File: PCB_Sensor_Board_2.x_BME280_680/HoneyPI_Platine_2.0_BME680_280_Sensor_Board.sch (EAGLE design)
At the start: 4 parts

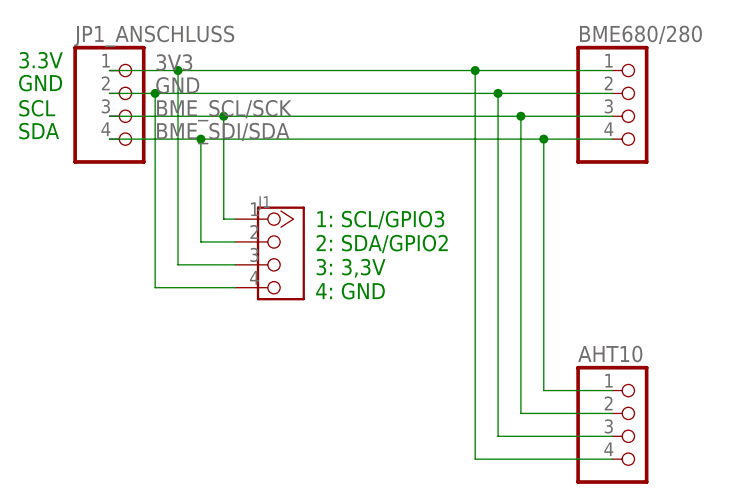
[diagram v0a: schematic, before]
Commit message: 3rd i²C interface
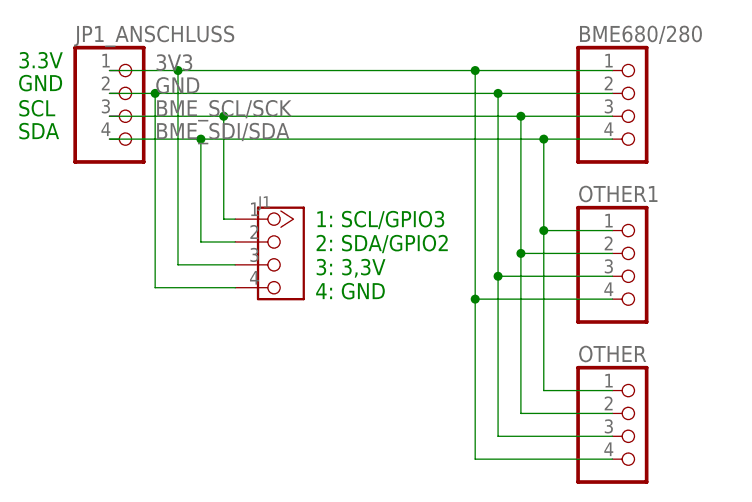
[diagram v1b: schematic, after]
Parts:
- added OTHER1: (no value), pinhead:PINHD-1X4
- renumbered AHT10 to OTHER
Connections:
- net 3V3: now also OTHER1.4
- net BME_SCL/SCK: now also OTHER1.2
- net BME_SDI/SDA: now also OTHER1.1
- net GND: now also OTHER1.3
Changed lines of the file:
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@@
 <part name="BME680/280" library="pinhead" library_urn="urn:adsk.eagle:library:325" deviceset="PINHD-1X4" device="" package3d_urn="urn:adsk.eagle:package:22407/2"/>
 <part name="JP1_ANSCHLUSS" library="pinhead" library_urn="urn:adsk.eagle:library:325" deviceset="PINHD-1X4" device="" package3d_urn="urn:adsk.eagle:package:22407/2"/>
-<part name="AHT10" library="pinhead" library_urn="urn:adsk.eagle:library:325" deviceset="PINHD-1X4" device="" package3d_urn="urn:adsk.eagle:package:22407/2"/>
+<part name="OTHER" library="pinhead" library_urn="urn:adsk.eagle:library:325" deviceset="PINHD-1X4" device="" package3d_urn="urn:adsk.eagle:package:22407/2"/>
 <part name="J1" library="Connector" deviceset="TWIG-4P-2.0" device="-2.0"/>
 <part name="FRAME1" library="frames" library_urn="urn:adsk.eagle:library:229" deviceset="DINA4_L" device=""/>
+<part name="OTHER1" library="pinhead" library_urn="urn:adsk.eagle:library:325" deviceset="PINHD-1X4" device="" package3d_urn="urn:adsk.eagle:package:22407/2"/>
 </parts>
 <sheets>
@@
 <attribute name="VALUE" x="-247.65" y="104.14" size="1.778" layer="96"/>
 </instance>
-<instance part="AHT10" gate="A" x="-185.42" y="76.2" smashed="yes" grouprefs="I²C-G1">
+<instance part="OTHER" gate="A" x="-185.42" y="76.2" smashed="yes" grouprefs="I²C-G1">
 <attribute name="NAME" x="-191.77" y="84.455" size="1.778" layer="95"/>
 <attribute name="VALUE" x="-191.77" y="68.58" size="1.778" layer="96"/>
@@
 <attribute name="DRAWING_NAME" x="-170.18" y="29.21" size="2.54" layer="94"/>
 </instance>
+<instance part="OTHER1" gate="A" x="-185.42" y="93.98" smashed="yes">
+<attribute name="NAME" x="-191.77" y="102.235" size="1.778" layer="95"/>
+<attribute name="VALUE" x="-191.77" y="86.36" size="1.778" layer="96"/>
+</instance>
 </instances>
 <busses>
@@
 <wire x1="-243.84" y1="111.76" x2="-231.14" y2="111.76" width="0.1524" layer="91" grouprefs="I²C-G1"/>
 <pinref part="BME680/280" gate="A" pin="3"/>
-<pinref part="AHT10" gate="A" pin="2"/>
+<pinref part="OTHER" gate="A" pin="2"/>
 <wire x1="-231.14" y1="111.76" x2="-198.12" y2="111.76" width="0.1524" layer="91" grouprefs="I²C-G1"/>
 <wire x1="-198.12" y1="111.76" x2="-187.96" y2="111.76" width="0.1524" layer="91" grouprefs="I²C-G1"/>
 <wire x1="-198.12" y1="78.74" x2="-187.96" y2="78.74" width="0.1524" layer="91" grouprefs="I²C-G1"/>
-<wire x1="-198.12" y1="78.74" x2="-198.12" y2="111.76" width="0.1524" layer="91" grouprefs="I²C-G1"/>
+<wire x1="-198.12" y1="78.74" x2="-198.12" y2="96.52" width="0.1524" layer="91" grouprefs="I²C-G1"/>
 <junction x="-198.12" y="111.76" grouprefs="I²C-G1"/>
 <pinref part="J1" gate="G$1" pin="1"/>
+<wire x1="-198.12" y1="96.52" x2="-198.12" y2="111.76" width="0.1524" layer="91" grouprefs="I²C-G1"/>
 <wire x1="-231.14" y1="111.76" x2="-231.14" y2="100.33" width="0.1524" layer="91" grouprefs="I²C-G1"/>
 <wire x1="-231.14" y1="100.33" x2="-229.87" y2="100.33" width="0.1524" layer="91" grouprefs="I²C-G1"/>
 <junction x="-231.14" y="111.76" grouprefs="I²C-G1"/>
+<pinref part="OTHER1" gate="A" pin="2"/>
+<wire x1="-187.96" y1="96.52" x2="-198.12" y2="96.52" width="0.1524" layer="91"/>
+<junction x="-198.12" y="96.52"/>
 </segment>
 </net>
@@
 <wire x1="-195.58" y1="109.22" x2="-233.68" y2="109.22" width="0.1524" layer="91" grouprefs="I²C-G1"/>
 <wire x1="-233.68" y1="109.22" x2="-243.84" y2="109.22" width="0.1524" layer="91" grouprefs="I²C-G1"/>
-<wire x1="-195.58" y1="109.22" x2="-195.58" y2="81.28" width="0.1524" layer="91" grouprefs="I²C-G1"/>
+<wire x1="-195.58" y1="109.22" x2="-195.58" y2="99.06" width="0.1524" layer="91" grouprefs="I²C-G1"/>
 <junction x="-195.58" y="109.22" grouprefs="I²C-G1"/>
-<pinref part="AHT10" gate="A" pin="1"/>
+<pinref part="OTHER" gate="A" pin="1"/>
+<wire x1="-195.58" y1="99.06" x2="-195.58" y2="81.28" width="0.1524" layer="91" grouprefs="I²C-G1"/>
 <wire x1="-195.58" y1="81.28" x2="-187.96" y2="81.28" width="0.1524" layer="91" grouprefs="I²C-G1"/>
 <pinref part="J1" gate="G$1" pin="2"/>
@@
 <wire x1="-233.68" y1="97.79" x2="-229.87" y2="97.79" width="0.1524" layer="91" grouprefs="I²C-G1"/>
 <junction x="-233.68" y="109.22" grouprefs="I²C-G1"/>
+<pinref part="OTHER1" gate="A" pin="1"/>
+<wire x1="-187.96" y1="99.06" x2="-195.58" y2="99.06" width="0.1524" layer="91"/>
+<junction x="-195.58" y="99.06"/>
 </segment>
 </net>
@@
 <wire x1="-187.96" y1="114.3" x2="-200.66" y2="114.3" width="0.1524" layer="91" grouprefs="I²C-G1"/>
 <pinref part="BME680/280" gate="A" pin="2"/>
-<pinref part="AHT10" gate="A" pin="3"/>
+<pinref part="OTHER" gate="A" pin="3"/>
 <wire x1="-200.66" y1="114.3" x2="-238.76" y2="114.3" width="0.1524" layer="91" grouprefs="I²C-G1"/>
 <wire x1="-238.76" y1="114.3" x2="-243.84" y2="114.3" width="0.1524" layer="91" grouprefs="I²C-G1"/>
-<wire x1="-200.66" y1="114.3" x2="-200.66" y2="76.2" width="0.1524" layer="91" grouprefs="I²C-G1"/>
+<wire x1="-200.66" y1="114.3" x2="-200.66" y2="93.98" width="0.1524" layer="91" grouprefs="I²C-G1"/>
+<wire x1="-200.66" y1="93.98" x2="-200.66" y2="76.2" width="0.1524" layer="91" grouprefs="I²C-G1"/>
 <wire x1="-200.66" y1="76.2" x2="-187.96" y2="76.2" width="0.1524" layer="91" grouprefs="I²C-G1"/>
 <junction x="-200.66" y="114.3" grouprefs="I²C-G1"/>
@@
 <pinref part="J1" gate="G$1" pin="4"/>
 <wire x1="-238.76" y1="92.71" x2="-229.87" y2="92.71" width="0.1524" layer="91" grouprefs="I²C-G1"/>
+<pinref part="OTHER1" gate="A" pin="3"/>
+<wire x1="-187.96" y1="93.98" x2="-200.66" y2="93.98" width="0.1524" layer="91"/>
+<junction x="-200.66" y="93.98"/>
 </segment>
 </net>
@@
 <wire x1="-236.22" y1="116.84" x2="-203.2" y2="116.84" width="0.1524" layer="91" grouprefs="I²C-G1"/>
 <wire x1="-203.2" y1="116.84" x2="-187.96" y2="116.84" width="0.1524" layer="91" grouprefs="I²C-G1"/>
-<wire x1="-203.2" y1="116.84" x2="-203.2" y2="73.66" width="0.1524" layer="91" grouprefs="I²C-G1"/>
+<wire x1="-203.2" y1="116.84" x2="-203.2" y2="91.44" width="0.1524" layer="91" grouprefs="I²C-G1"/>
 <junction x="-203.2" y="116.84" grouprefs="I²C-G1"/>
-<pinref part="AHT10" gate="A" pin="4"/>
+<pinref part="OTHER" gate="A" pin="4"/>
+<wire x1="-203.2" y1="91.44" x2="-203.2" y2="73.66" width="0.1524" layer="91" grouprefs="I²C-G1"/>
 <wire x1="-203.2" y1="73.66" x2="-187.96" y2="73.66" width="0.1524" layer="91" grouprefs="I²C-G1"/>
 <pinref part="J1" gate="G$1" pin="3"/>
@@
 <wire x1="-236.22" y1="95.25" x2="-229.87" y2="95.25" width="0.1524" layer="91" grouprefs="I²C-G1"/>
 <junction x="-236.22" y="116.84" grouprefs="I²C-G1"/>
+<pinref part="OTHER1" gate="A" pin="4"/>
+<wire x1="-187.96" y1="91.44" x2="-203.2" y2="91.44" width="0.1524" layer="91"/>
+<junction x="-203.2" y="91.44"/>
 </segment>
 </net>

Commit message: Updates, updates...
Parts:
- added GND: (no value), pinhead:PINHD-1X4
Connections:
- net GND: now also GND.1, GND.2, GND.3, GND.4
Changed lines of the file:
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@@
 <clearance class="0" value="0.3048"/>
 </class>
-<class number="1" name="Supply3v3" width="0.2032" drill="0">
+<class number="1" name="Supply3v3" width="0.25" drill="0">
 <clearance class="1" value="0.3048"/>
 </class>
-<class number="2" name="Supply5v" width="0.4064" drill="0">
+<class number="2" name="Supply5v" width="0.5" drill="0">
 <clearance class="2" value="0.3048"/>
 </class>
@@
 <part name="FRAME1" library="frames" library_urn="urn:adsk.eagle:library:229" deviceset="DINA4_L" device=""/>
 <part name="OTHER1" library="pinhead" library_urn="urn:adsk.eagle:library:325" deviceset="PINHD-1X4" device="" package3d_urn="urn:adsk.eagle:package:22407/2"/>
+<part name="GND" library="pinhead" library_urn="urn:adsk.eagle:library:325" deviceset="PINHD-1X4" device="" package3d_urn="urn:adsk.eagle:package:22407/2"/>
 </parts>
 <sheets>
@@
 <attribute name="NAME" x="-191.77" y="102.235" size="1.778" layer="95"/>
 <attribute name="VALUE" x="-191.77" y="86.36" size="1.778" layer="96"/>
+</instance>
+<instance part="GND" gate="A" x="-220.98" y="78.74" smashed="yes">
+<attribute name="NAME" x="-227.33" y="86.995" size="1.778" layer="95"/>
+<attribute name="VALUE" x="-227.33" y="71.12" size="1.778" layer="96"/>
 </instance>
 </instances>
@@
 </segment>
 </net>
-<net name="GND" class="1">
+<net name="GND" class="2">
 <segment>
 <label x="-238.76" y="114.3" size="1.778" layer="95" grouprefs="I²C-G1"/>
@@
 <wire x1="-187.96" y1="93.98" x2="-200.66" y2="93.98" width="0.1524" layer="91"/>
 <junction x="-200.66" y="93.98"/>
+<wire x1="-238.76" y1="92.71" x2="-238.76" y2="83.82" width="0.1524" layer="91"/>
+<pinref part="GND" gate="A" pin="1"/>
+<wire x1="-238.76" y1="83.82" x2="-223.52" y2="83.82" width="0.1524" layer="91"/>
+<pinref part="GND" gate="A" pin="2"/>
+<wire x1="-238.76" y1="83.82" x2="-238.76" y2="81.28" width="0.1524" layer="91"/>
+<wire x1="-238.76" y1="81.28" x2="-223.52" y2="81.28" width="0.1524" layer="91"/>
+<junction x="-238.76" y="83.82"/>
+<pinref part="GND" gate="A" pin="3"/>
+<wire x1="-238.76" y1="81.28" x2="-238.76" y2="78.74" width="0.1524" layer="91"/>
+<wire x1="-238.76" y1="78.74" x2="-223.52" y2="78.74" width="0.1524" layer="91"/>
+<junction x="-238.76" y="81.28"/>
+<pinref part="GND" gate="A" pin="4"/>
+<wire x1="-238.76" y1="78.74" x2="-238.76" y2="76.2" width="0.1524" layer="91"/>
+<wire x1="-238.76" y1="76.2" x2="-223.52" y2="76.2" width="0.1524" layer="91"/>
+<junction x="-238.76" y="78.74"/>
 </segment>
 </net>
-<net name="3V3" class="0">
+<net name="3V3" class="1">
 <segment>
 <label x="-238.76" y="116.84" size="1.778" layer="95" grouprefs="I²C-G1"/>
